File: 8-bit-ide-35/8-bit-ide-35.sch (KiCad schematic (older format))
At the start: 7 parts, among them U1 ATmega328P-PU, U2 GAL22V10, U3 74LS299

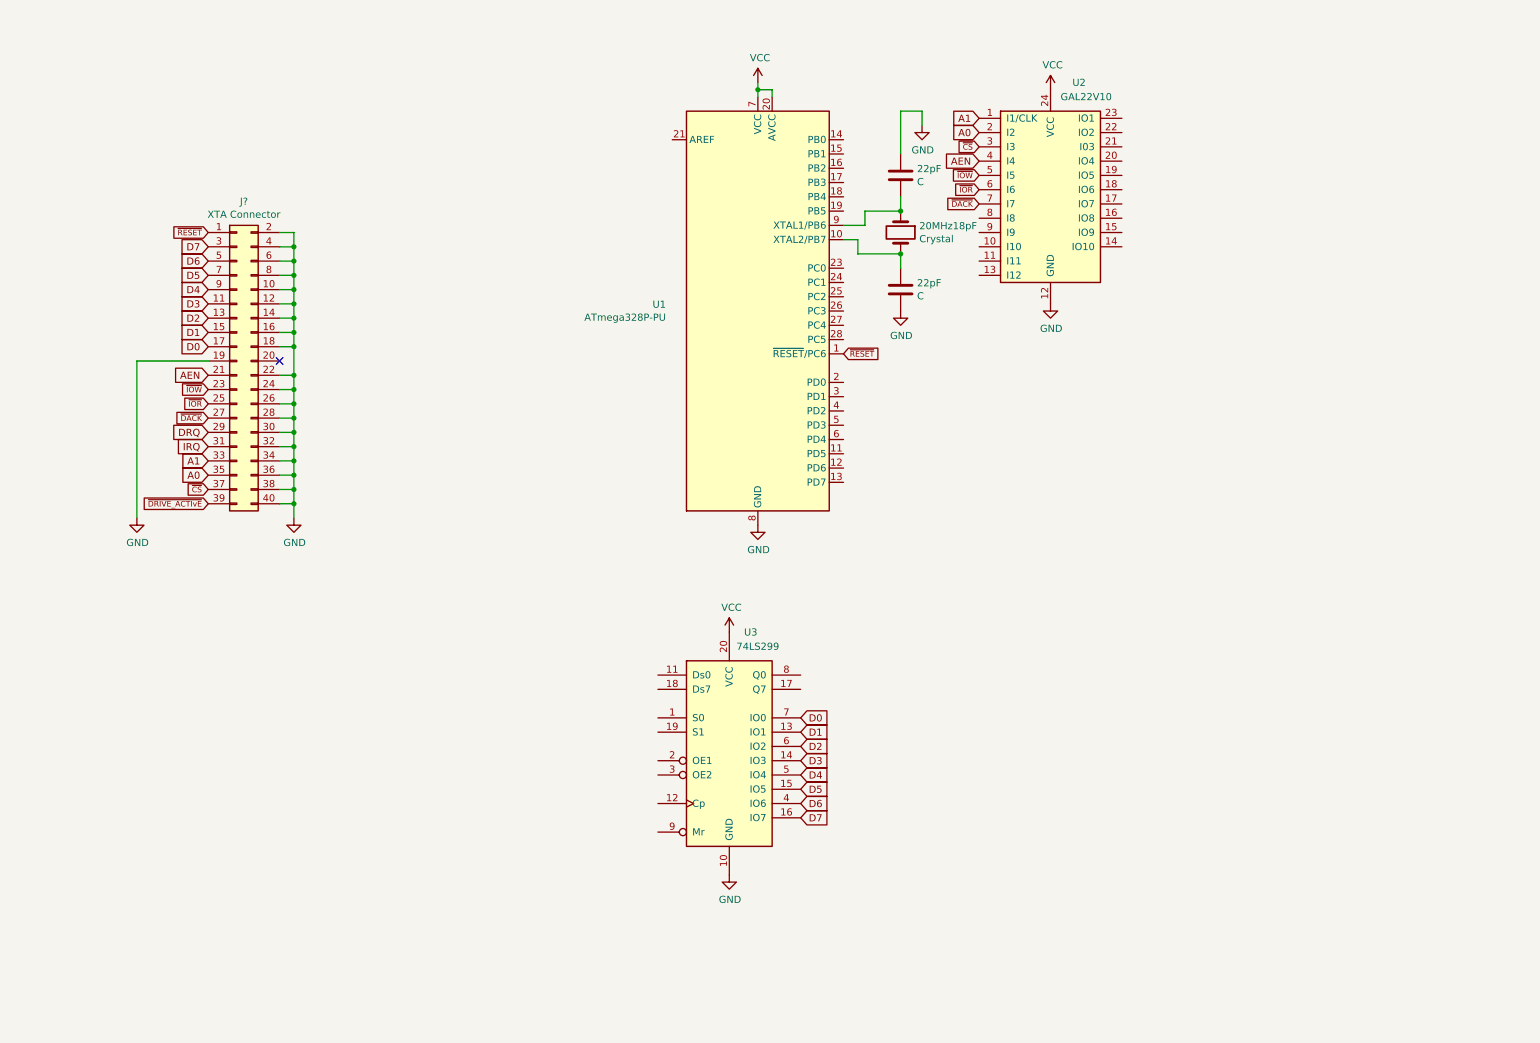
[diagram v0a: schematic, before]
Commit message: Start redoing schematic. Add library symbols for XTA and IBM interfaces.
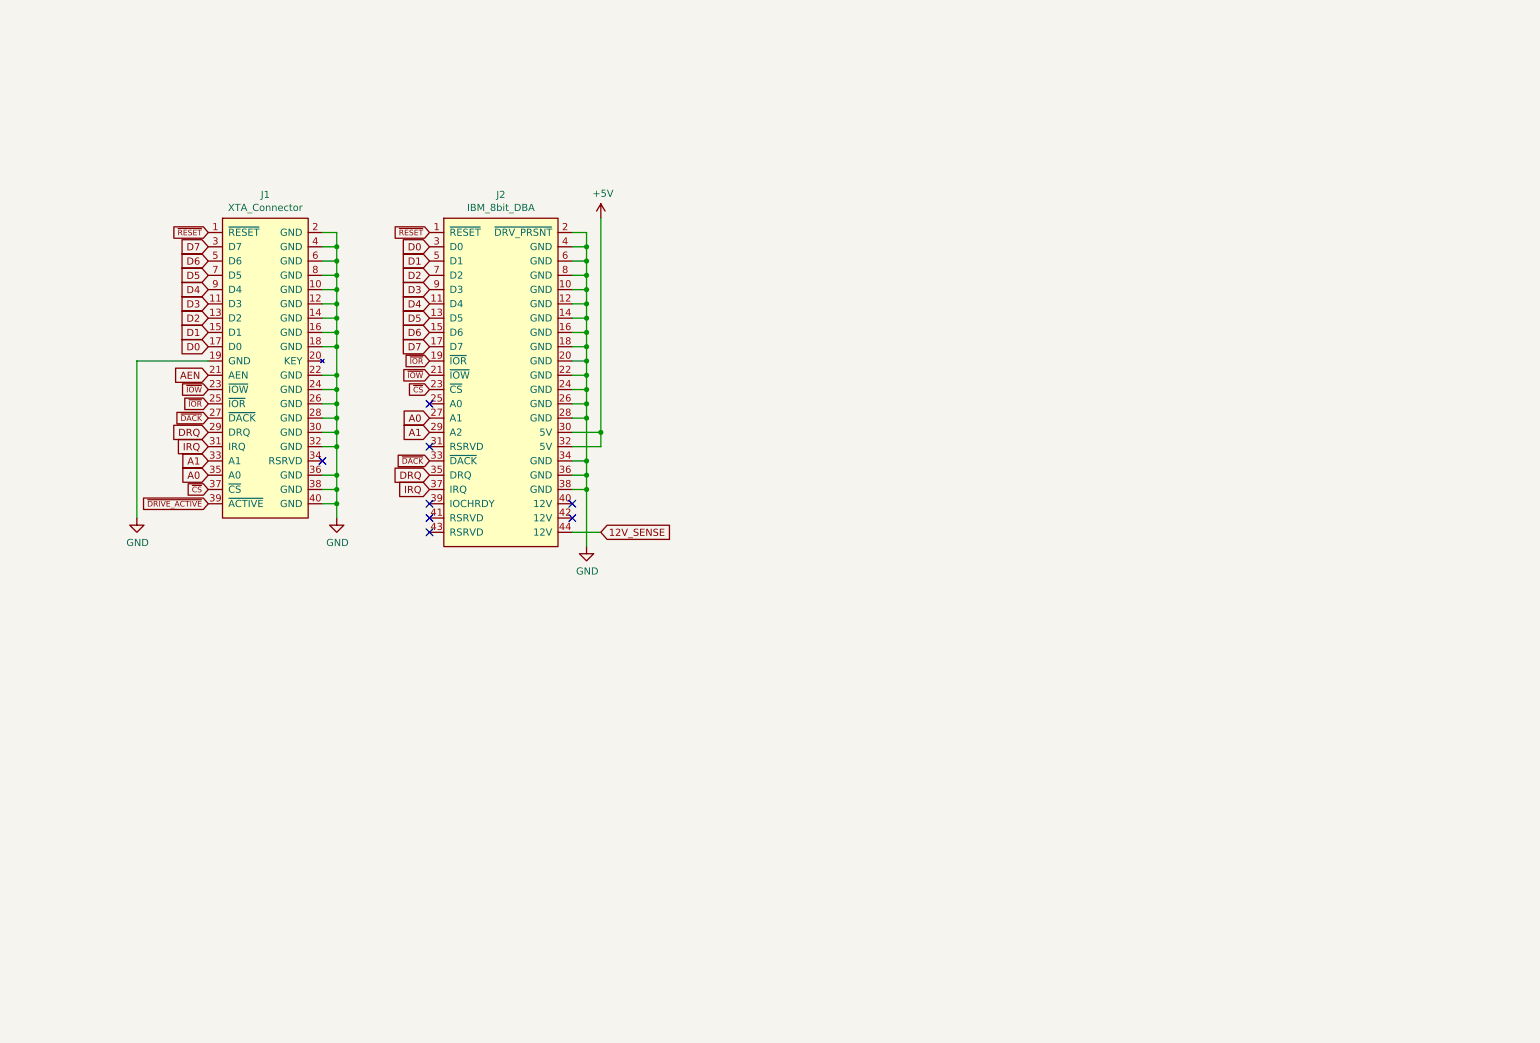
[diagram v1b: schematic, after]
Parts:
- removed 20MHz18pF: Crystal, symbol Device:Crystal
- removed 22pF (x2): C, symbol Device:C
- removed J?: XTA Connector, symbol Connector_Generic:Conn_02x20_Odd_Even
- removed U1: ATmega328P-PU, Package_DIP:DIP-28_W7.62mm, symbol MCU_Microchip_ATmega:ATmega328P-PU
- removed U2: GAL22V10, symbol 00Custom:GAL22V10
- removed U3: 74LS299, symbol 74xx:74LS299
- added J1: XTA_Connector, symbol 00Custom:XTA_Connector
- added J2: IBM_8bit_DBA, symbol 00Custom:IBM_8bit_DBA
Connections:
- net A0: now also J1.35 (A0), J2.27 (A1)
- net A1: now also J1.33 (A1), J2.29 (A2)
- net AEN: now also J1.21 (AEN)
- net D0: now also J1.17 (D0), J2.3 (D0)
- net D1: now also J1.15 (D1), J2.5 (D1)
- net D2: now also J1.13 (D2), J2.7 (D2)
- net D3: now also J1.11 (D3), J2.9 (D3)
- net D4: now also J1.9 (D4), J2.11 (D4)
- net D5: now also J1.7 (D5), J2.13 (D5)
- net D6: now also J1.5 (D6), J2.15 (D6)
- net D7: now also J1.3 (D7), J2.17 (D7)
- net DRQ: now also J1.29 (DRQ), J2.35 (DRQ)
- net GND: now also J1.10 (GND), J1.12 (GND), J1.14 (GND), J1.16 (GND), J1.18 (GND), J1.19 (GND), J1.2 (GND), J1.22 (GND), J1.24 (GND), J1.26 (GND), J1.28 (GND), J1.30 (GND), J1.32 (GND), J1.36 (GND), J1.38 (GND), J1.4 (GND), J1.40 (GND), J1.6 (GND), J1.8 (GND), J2.10 (GND), J2.12 (GND), J2.14 (GND), J2.16 (GND), J2.18 (GND), J2.2 (~DRV_PRSNT), J2.20 (GND), J2.22 (GND), J2.24 (GND), J2.26 (GND), J2.28 (GND), J2.34 (GND), J2.36 (GND), J2.38 (GND), J2.4 (GND), J2.6 (GND), J2.8 (GND)
- net IRQ: now also J1.31 (IRQ), J2.37 (IRQ)
- net ~CS: now also J1.37 (~CS), J2.23 (~CS)
- net ~DACK: now also J1.27 (~DACK), J2.33 (~DACK)
- net ~IOR: now also J1.25 (~IOR), J2.19 (~IOR)
- net ~IOW: now also J1.23 (~IOW), J2.21 (~IOW)
- net ~RESET: now also J1.1 (~RESET), J2.1 (~RESET)
- new net +5V: J2.30 (5V), J2.32 (5V)
- new net 12V_SENSE: J2.44 (12V)
- new net ~DRIVE_ACTIVE: J1.39 (~ACTIVE)
- no-connect marks 1 -> 8

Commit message: Add symbol for RPi Pico, do more schematic work.
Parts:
- added D?: D_Schottky, symbol Device:D_Schottky
- added J?: XTA Power, symbol Connector_Generic:Conn_01x04
- added J?: LED, symbol Connector_Generic:Conn_01x02
- added R? (x2): 120R, Resistor_SMD:R_1206_3216Metric, symbol Device:R
- added R? (x4): 10K, Resistor_SMD:R_1206_3216Metric, symbol Device:R
- added SW?: Reset, symbol Switch:SW_Push
- added U?: RPI_PICO, symbol 00Custom:RPI_PICO
- added U? (x2): 74LVC245, symbol 74xx:74LS245
- added U? (x5): 74LS125, symbol 74xx:74LS125
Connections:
- net +5V: now also D?.1 (K), R?.1, U?.12, U?.14 (VCC), U?.39 (VSYS), U?.9; no longer J2.30 (5V), J2.32 (5V)
- net A0: now also U?.2 (A0)
- net A1: now also U?.3 (A1)
- net AEN: now also U?.4 (A2)
- net D0: now also U?.2 (A0)
- net D1: now also U?.3 (A1)
- net D2: now also U?.4 (A2)
- net D3: now also U?.5 (A3)
- net D4: now also U?.6 (A4)
- net D5: now also U?.7 (A5)
- net D6: now also U?.8 (A6)
- net D7: now also U?.9 (A7)
- net DRQ: now also U?.8
- net GND: now also J?.2 (Pin_2), J?.3 (Pin_3), R?.2, SW?.2, U?.1 (A->B), U?.10 (GND), U?.10 (GND), U?.13 (GND), U?.18 (GND), U?.19 (CE), U?.19 (CE), U?.2, U?.23 (GND), U?.28 (GND), U?.3 (GND), U?.33 (GND), U?.38 (GND), U?.5, U?.7 (GND), U?.8 (GND)
- net IRQ: now also U?.11
- net ~CS: now also U?.6 (A4)
- net ~DACK: now also U?.5 (A3)
- net ~DRIVE_ACTIVE: now also U?.3
- net ~IOR: now also U?.8 (A6)
- net ~IOW: now also U?.9 (A7)
- net ~RESET: now also U?.7 (A5)
- net 12V_SENSE renamed IBM_SENSE_12V
- net IBM_SENSE_12V: now also R?.1
- new net: SW?.1, U?.30 (RUN)
- new net: J?.2 (Pin_2), R?.1
- new net: R?.2, U?.6
- new net: J?.1 (Pin_1), R?.2
- new net: R?.1, R?.2 (x2)
- new net +3V3: U?.20 (VCC), U?.20 (VCC), U?.36 (3V3)
- new net 5V_POWER_IN: D?.2 (A), J2.30 (5V), J2.32 (5V), J?.4 (Pin_4)
- new net A0_3V3: U?.11 (GP8), U?.18 (B0)
- new net A1_3V3: U?.12 (GP9), U?.17 (B1)
- new net AEN_3V3: U?.14 (GP10), U?.16 (B2)
- new net D0_3V3: U?.1 (GP0), U?.18 (B0)
- new net D1_3V3: U?.17 (B1), U?.2 (GP1)
- new net D2_3V3: U?.16 (B2), U?.4 (GP2)
- new net D3_3V3: U?.15 (B3), U?.5 (GP3)
- new net D4_3V3: U?.14 (B4), U?.6 (GP4)
- new net D5_3V3: U?.13 (B5), U?.7 (GP5)
- new net D6_3V3: U?.12 (B6), U?.9 (GP6)
- new net D7_3V3: U?.10 (GP7), U?.11 (B7)
- new net DATA_DIR: U?.1 (A->B), U?.24 (GP18)
- new net IBM_SENSE_3V3: R?.1, R?.2, U?.34 (GP28)
- new net ~CS~_3V3: U?.14 (B4), U?.21 (GP16)
- new net ~DACK~_3V3: U?.15 (B3), U?.15 (GP11)
- new net ~DRIVE_ACTIVE~_3V3: U?.1, U?.25 (GP19), U?.4
- new net ~DRQ~_3V3: U?.10, U?.16 (GP12)
- new net ~IOR~_3V3: U?.12 (B6), U?.19 (GP14)
- new net ~IOW~_3V3: U?.11 (B7), U?.20 (GP15)
- new net ~IRQ~_3V3: U?.13, U?.17 (GP13)
- new net ~RESET~_3V3: U?.13 (B5), U?.22 (GP17)
- no-connect marks 8 -> 12
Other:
- note added: "On GP26-28, there is a clamp diode\nto 3.3v so no external one is needed."
- moved on the sheet: J1, J2

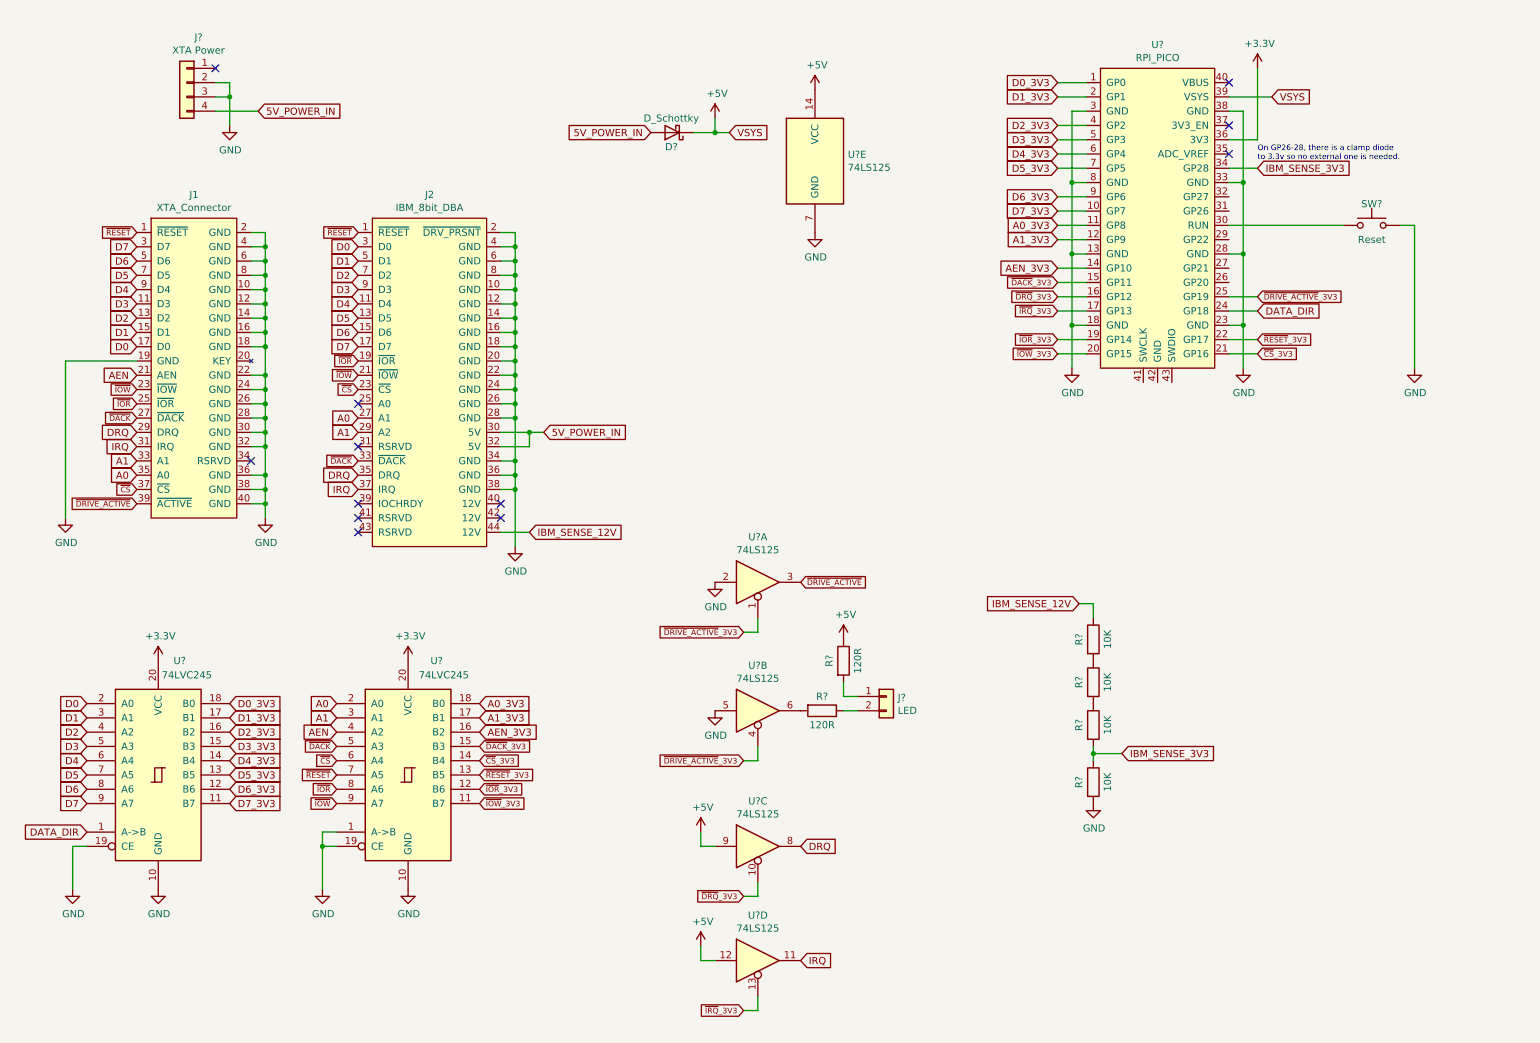
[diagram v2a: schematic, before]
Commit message: Mostly finish initial pass at schematic. Still needs SD connectors.
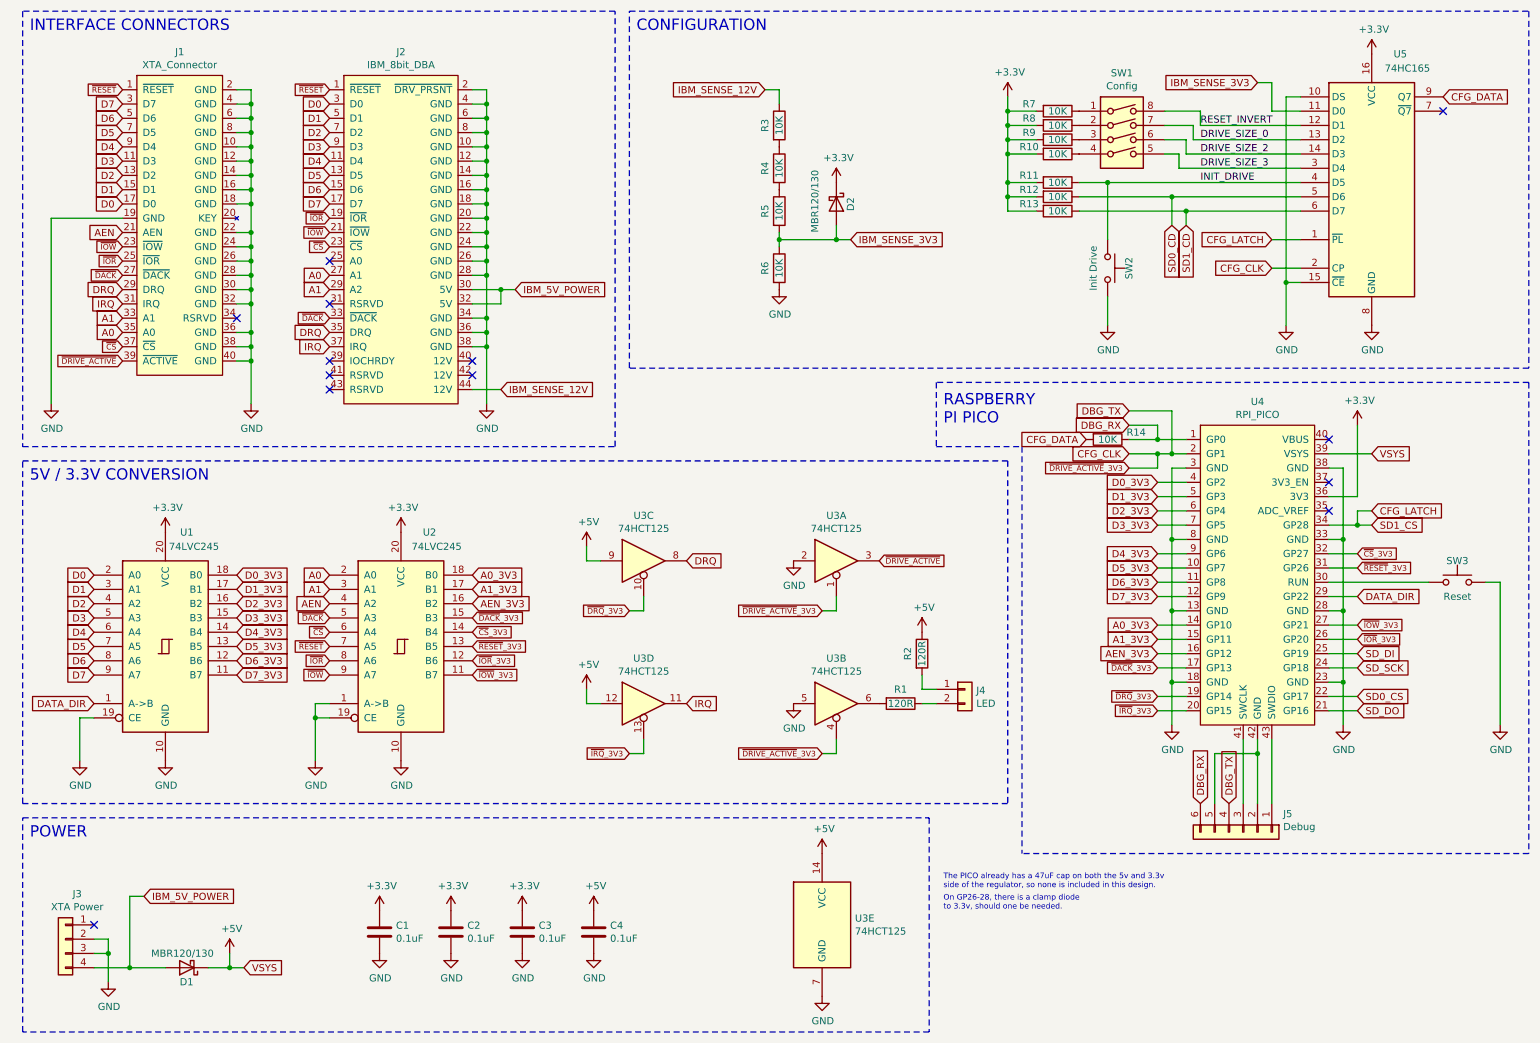
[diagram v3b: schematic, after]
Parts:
- added C1, C2, C3, C4: 0.1uF, Capacitor_SMD:C_1206_3216Metric, symbol Device:C
- added D2: MBR120/130, Diode_SMD:D_SOD-123, symbol Device:D_Schottky
- added J5: Debug, symbol Connector_Generic:Conn_01x06
- added R10, R11, R12, R13, R14, R7, R8, R9: 10K, Resistor_SMD:R_1206_3216Metric, symbol Device:R
- added SW1: Config, symbol Switch:SW_DIP_x04
- added SW2: Init Drive, symbol Switch:SW_Push
- added U5: 74HC165, symbol 74xx:74HC165
- D1: renamed from D?; value D_Schottky -> MBR120/130; footprint (none) -> Diode_SMD:D_SOD-123
- U3: renamed from U?; value 74LS125 -> 74HCT125
- gave numbers to parts that had none: 12
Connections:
- net +3V3: now also C1.1, C2.1, C3.1, D2.1 (K), R10.2, R11.2, R12.2, R13.2, R7.2, R8.2, R9.2, U5.16 (VCC)
- net +5V: now also C4.1
- net A0_3V3: now also U4.14 (GP10); no longer U4.11 (GP8)
- net A1_3V3: now also U4.15 (GP11); no longer U4.12 (GP9)
- net AEN_3V3: now also U4.16 (GP12); no longer U4.14 (GP10)
- net D0_3V3: now also U4.4 (GP2); no longer U4.1 (GP0)
- net D1_3V3: now also U4.5 (GP3); no longer U4.2 (GP1)
- net D2_3V3: now also U4.6 (GP4); no longer U4.4 (GP2)
- net D3_3V3: now also U4.7 (GP5); no longer U4.5 (GP3)
- net D4_3V3: now also U4.9 (GP6); no longer U4.6 (GP4)
- net D5_3V3: now also U4.10 (GP7); no longer U4.7 (GP5)
- net D6_3V3: now also U4.11 (GP8); no longer U4.9 (GP6)
- net D7_3V3: now also U4.12 (GP9); no longer U4.10 (GP7)
- net DATA_DIR: now also U4.29 (GP22); no longer U4.24 (GP18)
- net GND: now also C1.2, C2.2, C3.2, C4.2, SW2.2, U5.10 (DS), U5.15 (~CE), U5.8 (GND)
- net IBM_SENSE_3V3: now also D2.2 (A), U5.11 (D0); no longer U4.34 (GP28)
- net ~CS~_3V3: now also U4.32 (GP27); no longer U4.21 (GP16)
- net ~DACK~_3V3: now also U4.17 (GP13); no longer U4.15 (GP11)
- net ~DRQ~_3V3: now also U4.19 (GP14); no longer U4.16 (GP12)
- net ~IOR~_3V3: now also U4.26 (GP20); no longer U4.19 (GP14)
- net ~IOW~_3V3: now also U4.27 (GP21); no longer U4.20 (GP15)
- net ~IRQ~_3V3: now also U4.20 (GP15); no longer U4.17 (GP13)
- net ~RESET~_3V3: now also U4.31 (GP26); no longer U4.22 (GP17)
- net at U4.41 (SWCLK): now also J5.3 (Pin_3)
- net at U4.42 (GND): now also J5.2 (Pin_2), J5.5 (Pin_5)
- net at U4.43 (SWDIO): now also J5.1 (Pin_1)
- net 5V_POWER_IN renamed IBM_5V_POWER
- net ~DRIVE_ACTIVE~_3V3 renamed CFG_CLK
- net CFG_CLK: now also U4.2 (GP1), J5.4 (Pin_4), U5.2 (CP); no longer U4.25 (GP19)
- new net: R7.1, SW1.1
- new net: R8.1, SW1.2
- new net: R9.1, SW1.3
- new net: R10.1, SW1.4
- new net CFG_DATA: R14.2, U5.9 (Q7)
- new net CFG_LATCH: U4.34 (GP28), U5.1 (~PL)
- new net DBG_RX: J5.6 (Pin_6), R14.1, U4.1 (GP0)
- new net DRIVE_SIZE_0: SW1.7, U5.13 (D2)
- new net DRIVE_SIZE_2: SW1.6, U5.14 (D3)
- new net DRIVE_SIZE_3: SW1.5, U5.3 (D4)
- new net INIT_DRIVE: R11.1, SW2.1, U5.4 (D5)
- new net RESET_INVERT: SW1.8, U5.12 (D1)
- new net SD0_CD: R12.1, U5.5 (D6)
- new net SD0_CS: U4.22 (GP17)
- new net SD1_CD: R13.1, U5.6 (D7)
- new net SD_DI: U4.25 (GP19)
- new net SD_DO: U4.21 (GP16)
- new net SD_SCK: U4.24 (GP18)
- no-connect marks 12 -> 13
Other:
- note added: "5V / 3.3V CONVERSION"
- note added: "CONFIGURATION"
- note added: "INTERFACE CONNECTORS"
- note added: "On GP26-28, there is a clamp diode\nto 3.3v, should one be needed."
- note added: "POWER"
- note added: "RASPBERRY\nPI PICO"
- note added: "The PICO already has a 47uF cap on both the 5v and 3.3v\nside of the regulator, so none is included in this design."
- note removed: "On GP26-28, there is a clamp diode\nto 3.3v so no external one is needed."
- moved on the sheet: D1, J1, J2, J3, J4, R1, R2, R3, R4, R5, R6, SW3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

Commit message: Add Pico design files and set up on a pcb.
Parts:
- U4: footprint (none) -> Pico:RPi_Pico_SMD_TH
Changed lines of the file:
@@
 F 0 "U4" H 9200 5615 50  0000 C CNN
 F 1 "RPI_PICO" H 9200 5524 50  0000 C CNN
-F 2 "" H 9200 5450 50  0001 C CNN
+F 2 "Pico:RPi_Pico_SMD_TH" H 9200 5450 50  0001 C CNN
 F 3 "" H 9200 5450 50  0001 C CNN
 	1    9200 4450
